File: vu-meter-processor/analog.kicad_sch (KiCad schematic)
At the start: 31 parts, among them U1 LM2904

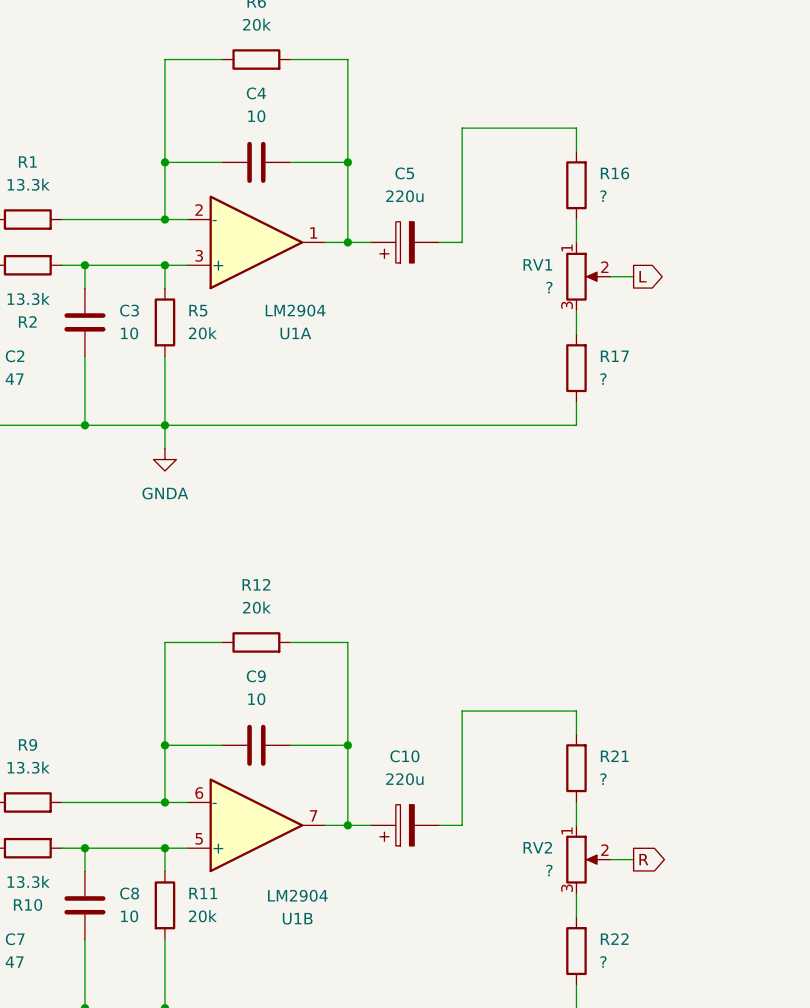
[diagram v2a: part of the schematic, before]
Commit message: fix: remove dc blocking capacitors
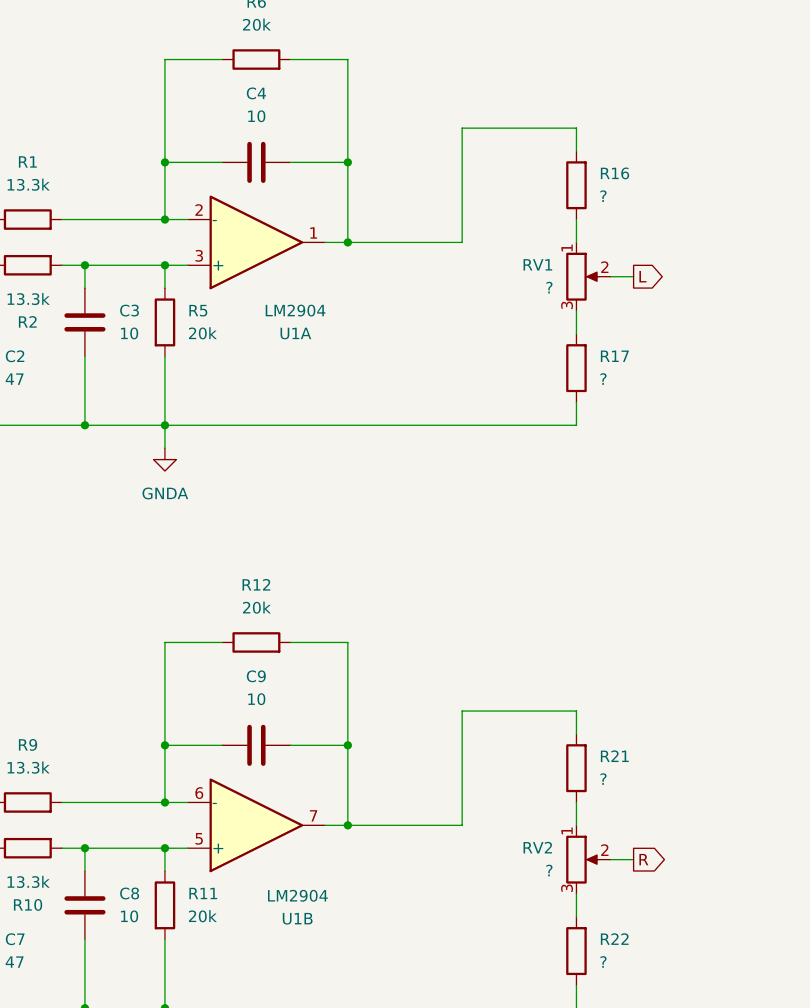
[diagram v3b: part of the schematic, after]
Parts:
- removed C10, C5: 220u, Capacitor_THT:CP_Radial_D8.0mm_P3.50mm, symbol Device:C_Polarized
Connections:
- net at C9.2, R12.2, U1.7: now also R21.2
- net at C4.2, R6.2, U1.1: now also R16.2
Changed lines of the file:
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@@
 	(wire
 		(pts
-			(xy 113.03 64.77) (xy 115.57 64.77)
+			(xy 113.03 64.77) (xy 125.73 64.77)
 		)
 		(stroke
@@
 	(wire
 		(pts
-			(xy 113.03 129.54) (xy 115.57 129.54)
+			(xy 113.03 129.54) (xy 125.73 129.54)
 		)
 		(stroke
@@
 	(wire
 		(pts
-			(xy 123.19 129.54) (xy 125.73 129.54)
-		)
-		(stroke
-			(width 0)
-			(type default)
-		)
-	)
-	(wire
-		(pts
 			(xy 92.71 44.45) (xy 92.71 55.88)
 		)
@@
 		(pts
 			(xy 92.71 149.86) (xy 83.82 149.86)
-		)
-		(stroke
-			(width 0)
-			(type default)
-		)
-	)
-	(wire
-		(pts
-			(xy 123.19 64.77) (xy 125.73 64.77)
 		)
 		(stroke
@@
 	)
 	(symbol
-		(lib_id "Device:C_Polarized")
-		(at 119.38 129.54 90)
-		(unit 1)
-		(exclude_from_sim no)
-		(in_bom yes)
-		(on_board yes)
-		(dnp no)
-		(property "Reference" "C10"
-			(at 119.38 121.92 90)
-			(effects
-				(font
-					(size 1.27 1.27)
-				)
-			)
-		)
-		(property "Value" "220u"
-			(at 119.38 124.46 90)
-			(effects
-				(font
-					(size 1.27 1.27)
-				)
-			)
-		)
-		(property "Footprint" "Capacitor_THT:CP_Radial_D8.0mm_P3.50mm"
-			(at 123.19 128.5748 0)
-			(effects
-				(font
-					(size 1.27 1.27)
-				)
-				(hide yes)
-			)
-		)
-		(property "Datasheet" "~"
-			(at 119.38 129.54 0)
-			(effects
-				(font
-					(size 1.27 1.27)
-				)
-				(hide yes)
-			)
-		)
-		(property "Description" "Polarized capacitor"
-			(at 119.38 129.54 0)
-			(effects
-				(font
-					(size 1.27 1.27)
-				)
-				(hide yes)
-			)
-		)
-		(property "Sim.Device" ""
-			(at 119.38 129.54 0)
-			(effects
-				(font
-					(size 1.27 1.27)
-				)
-			)
-		)
-		(property "Sim.Pins" ""
-			(at 119.38 129.54 0)
-			(effects
-				(font
-					(size 1.27 1.27)
-				)
-			)
-		)
-		(pin "1"
-		)
-		(pin "2"
-		)
-		(instances
-			(project "vu-meter-processor"
-				(path "/50201dbb-ce2c-4681-8d0b-b3063868b684/b5a15edd-f079-4332-a725-9b2801ef9020"
-					(reference "C10")
-					(unit 1)
-				)
-			)
-		)
-	)
-	(symbol
 		(lib_id "Device:R")
 		(at 77.47 127 90)
@@
 					(unit 1)
 				)
-			)
-		)
-	)
-	(symbol
-		(lib_id "Device:C_Polarized")
-		(at 119.38 64.77 90)
-		(unit 1)
-		(exclude_from_sim no)
-		(in_bom yes)
-		(on_board yes)
-		(dnp no)
-		(property "Reference" "C5"
-			(at 119.38 57.15 90)
-			(effects
-				(font
-					(size 1.27 1.27)
-				)
-			)
-		)
-		(property "Value" "220u"
-			(at 119.38 59.69 90)
-			(effects
-				(font
-					(size 1.27 1.27)
-				)
-			)
-		)
-		(property "Footprint" "Capacitor_THT:CP_Radial_D8.0mm_P3.50mm"
-			(at 123.19 63.8048 0)
-			(effects
-				(font
-					(size 1.27 1.27)
-				)
-				(hide yes)
-			)
-		)
-		(property "Datasheet" "~"
-			(at 119.38 64.77 0)
-			(effects
-				(font
-					(size 1.27 1.27)
-				)
-				(hide yes)
-			)
-		)
-		(property "Description" "Polarized capacitor"
-			(at 119.38 64.77 0)
-			(effects
-				(font
-					(size 1.27 1.27)
-				)
-				(hide yes)
-			)
-		)
-		(property "Sim.Device" ""
-			(at 119.38 64.77 0)
-			(effects
-				(font
-					(size 1.27 1.27)
-				)
-			)
-		)
-		(property "Sim.Pins" ""
-			(at 119.38 64.77 0)
-			(effects
-				(font
-					(size 1.27 1.27)
-				)
-			)
-		)
-		(pin "1"
-		)
-		(pin "2"
-		)
-		(instances
-			(project "vu-meter-processor"
-				(path "/50201dbb-ce2c-4681-8d0b-b3063868b684/b5a15edd-f079-4332-a725-9b2801ef9020"
-					(reference "C5")
-					(unit 1)
-				)
